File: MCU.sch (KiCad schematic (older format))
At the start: 18 parts, among them U4 STM32F303RETx

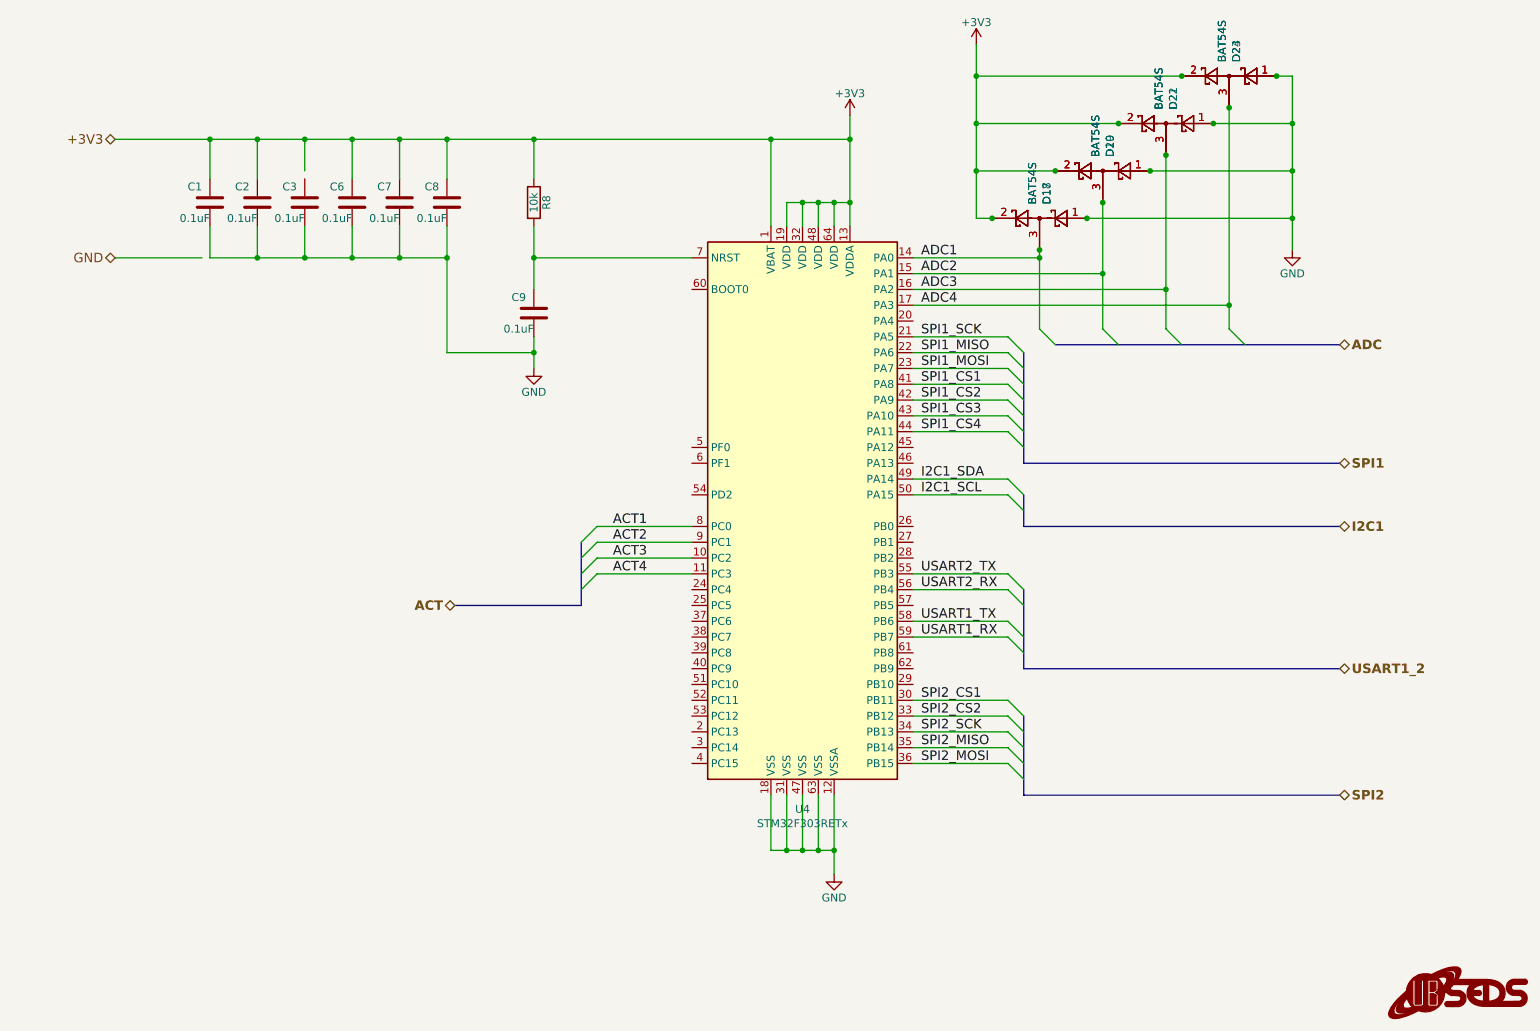
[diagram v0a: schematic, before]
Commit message: Updated pinmap
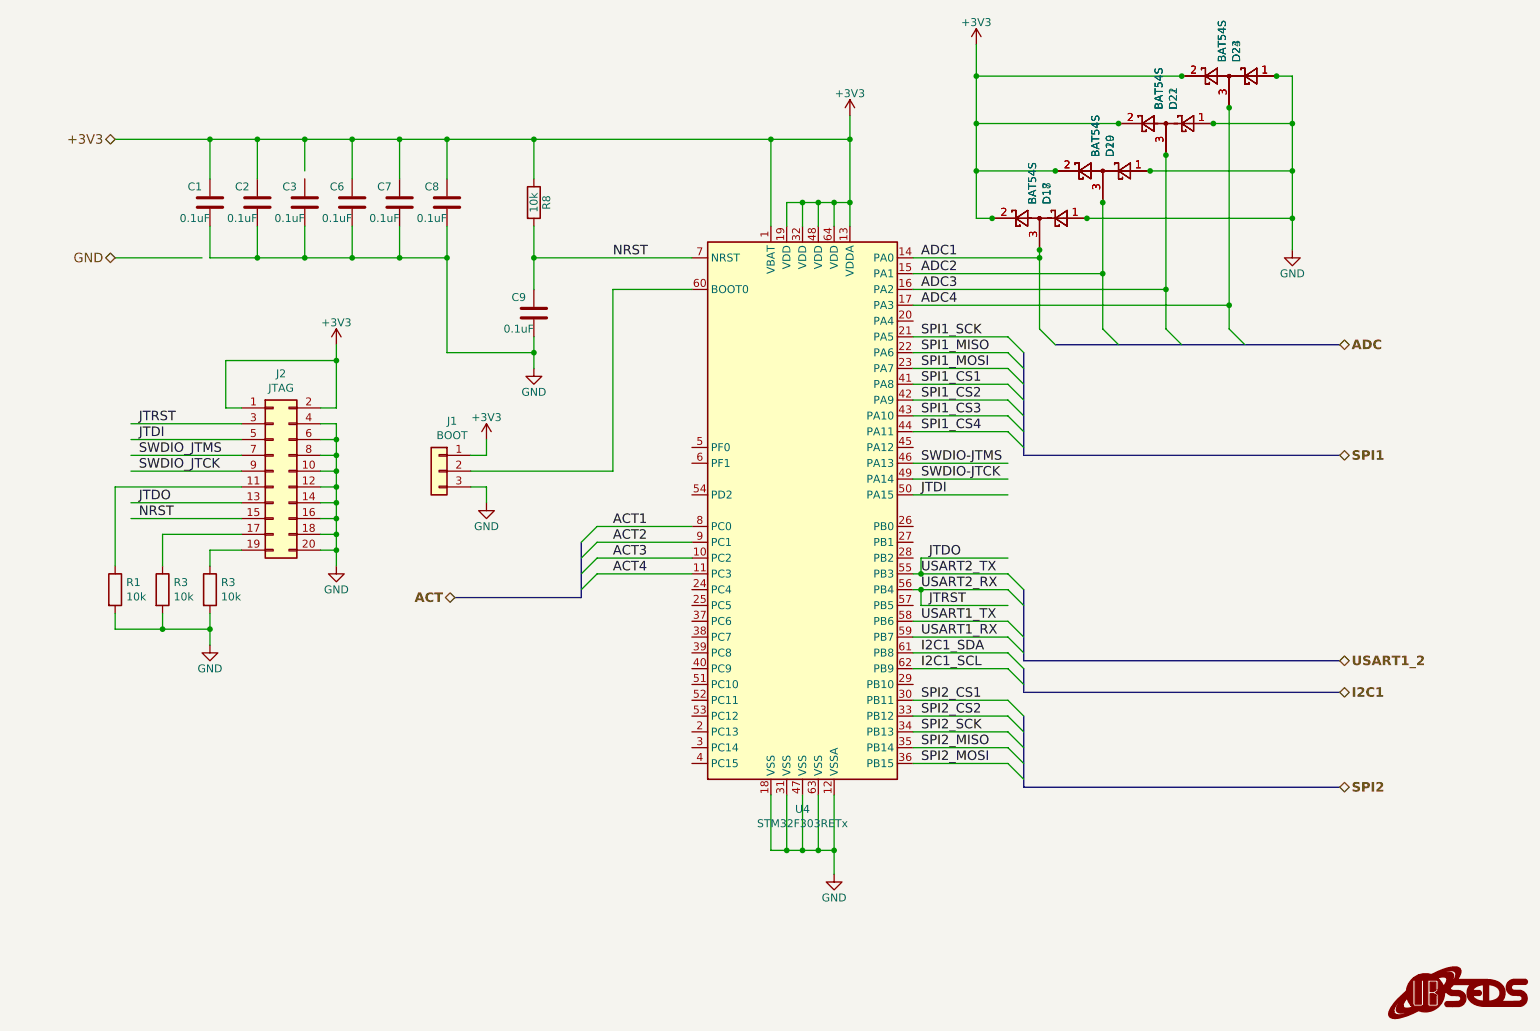
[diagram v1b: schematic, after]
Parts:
- added J1: BOOT, symbol Connector_Generic:Conn_01x03
- added J2: JTAG, symbol Connector_Generic:Conn_02x10_Odd_Even
- added R1, R3 (x2): 10k, symbol Device:R
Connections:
- net labels added: JTDI, JTDO, JTRST, NRST, SWDIO-JTCK, SWDIO-JTMS, SWDIO_JTCK, SWDIO_JTMS
- wire segments 107 -> 165

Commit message: Starting to fix ERC errors
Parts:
- C3: renamed from C1; footprint (none) -> Capacitor_SMD:C_0603_1608Metric_Pad1.05x0.95mm_HandSolder
- C4: renamed from C2; footprint (none) -> Capacitor_SMD:C_0603_1608Metric_Pad1.05x0.95mm_HandSolder
- C5: renamed from C3; footprint (none) -> Capacitor_SMD:C_0603_1608Metric_Pad1.05x0.95mm_HandSolder
- C6, C7, C8, C9: footprint (none) -> Capacitor_SMD:C_0603_1608Metric_Pad1.05x0.95mm_HandSolder
- J2: footprint (none) -> Connector_PinHeader_2.54mm:PinHeader_2x10_P2.54mm_Vertical
- J3: renamed from J1; footprint (none) -> Connector_PinHeader_2.54mm:PinHeader_1x03_P2.54mm_Vertical
- R5: renamed from R1; footprint (none) -> Resistor_SMD:R_1206_3216Metric_Pad1.42x1.75mm_HandSolder
- R6, R7: renamed from R3; footprint (none) -> Resistor_SMD:R_1206_3216Metric_Pad1.42x1.75mm_HandSolder
- R8: footprint Resistor_THT:R_Axial_DIN0207_L6.3mm_D2.5mm_P10.16mm_Horizontal -> Resistor_SMD:R_1206_3216Metric_Pad1.42x1.75mm_HandSolder
- renumbered D17 to D1, D18 to D2, D19 to D3, D20 to D4, D21 to D5, D22 to D6, D23 to D7, D24 to D8, U4 to U6
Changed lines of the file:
@@
 $Descr USLetter 11000 8500
 encoding utf-8
-Sheet 3 3
+Sheet 2 3
 Title "Flight Computer"
 Date ""
@@
 $EndComp
 $Comp
-L MCU_ST_STM32F3:STM32F303RETx U4
+L MCU_ST_STM32F3:STM32F303RETx U6
 U 1 1 5DF0B287
 P 5700 4050
-F 0 "U4" H 5700 2161 50  0000 C CNN
+F 0 "U6" H 5700 2161 50  0000 C CNN
 F 1 "STM32F303RETx" H 5700 2070 50  0000 C CNN
 F 2 "Package_QFP:LQFP-64_10x10mm_P0.5mm" H 5100 2350 50  0001 R CNN
@@
 $EndComp
 $Comp
-L power:+3V3 #PWR0123
+L power:+3V3 #PWR030
 U 1 1 5DF125E2
 P 6000 1550
-F 0 "#PWR0123" H 6000 1400 50  0001 C CNN
+F 0 "#PWR030" H 6000 1400 50  0001 C CNN
 F 1 "+3V3" H 6000 1690 50  0000 C CNN
 F 2 "" H 6000 1550 50  0001 C CNN
@@
 $EndComp
 $Comp
-L power:GND #PWR0124
+L power:GND #PWR029
 U 1 1 5DF17C0F
 P 5900 6350
-F 0 "#PWR0124" H 5900 6100 50  0001 C CNN
+F 0 "#PWR029" H 5900 6100 50  0001 C CNN
 F 1 "GND" H 5900 6200 50  0000 C CNN
 F 2 "" H 5900 6350 50  0001 C CNN
@@
 	5500 1700 5500 2250
 $Comp
-L power:GND #PWR0125
+L power:GND #PWR028
 U 1 1 5DFA0210
 P 4000 3150
-F 0 "#PWR0125" H 4000 2900 50  0001 C CNN
+F 0 "#PWR028" H 4000 2900 50  0001 C CNN
 F 1 "GND" H 4000 3000 50  0000 C CNN
 F 2 "" H 4000 3150 50  0001 C CNN
@@
 	7000 3550 7100 3650
 $Comp
-L Diode:BAT54S D19
+L Diode:BAT54S D3
 U 1 1 5E142556
 P 7600 1900
-F 0 "D19" V 7554 1988 50  0000 L CNN
+F 0 "D3" V 7554 1988 50  0000 L CNN
 F 1 "BAT54S" V 7645 1988 50  0000 L CNN
 F 2 "Package_TO_SOT_SMD:SOT-23" H 7675 2025 50  0001 L CNN
@@
 $EndComp
 $Comp
-L Diode:BAT54S D20
+L Diode:BAT54S D4
 U 1 1 5E14255C
 P 7600 1900
-F 0 "D20" V 7554 1988 50  0000 L CNN
+F 0 "D4" V 7554 1988 50  0000 L CNN
 F 1 "BAT54S" V 7645 1988 50  0000 L CNN
 F 2 "Package_TO_SOT_SMD:SOT-23" H 7675 2025 50  0001 L CNN
@@
 $EndComp
 $Comp
-L Diode:BAT54S D21
+L Diode:BAT54S D5
 U 1 1 5E211E6E
 P 8000 1600
-F 0 "D21" V 7954 1688 50  0000 L CNN
+F 0 "D5" V 7954 1688 50  0000 L CNN
 F 1 "BAT54S" V 8045 1688 50  0000 L CNN
 F 2 "Package_TO_SOT_SMD:SOT-23" H 8075 1725 50  0001 L CNN
@@
 $EndComp
 $Comp
-L Diode:BAT54S D22
+L Diode:BAT54S D6
 U 1 1 5E211E6F
 P 8000 1600
-F 0 "D22" V 7954 1688 50  0000 L CNN
+F 0 "D6" V 7954 1688 50  0000 L CNN
 F 1 "BAT54S" V 8045 1688 50  0000 L CNN
 F 2 "Package_TO_SOT_SMD:SOT-23" H 8075 1725 50  0001 L CNN
@@
 $EndComp
 $Comp
-L power:+3V3 #PWR0126
+L power:+3V3 #PWR031
 U 1 1 5E211E72
 P 6800 1100
-F 0 "#PWR0126" H 6800 950 50  0001 C CNN
+F 0 "#PWR031" H 6800 950 50  0001 C CNN
 F 1 "+3V3" H 6800 1240 50  0000 C CNN
 F 2 "" H 6800 1100 50  0001 C CNN
@@
 $EndComp
 $Comp
-L power:GND #PWR0127
+L power:GND #PWR032
 U 1 1 5E211E73
 P 8800 2400
-F 0 "#PWR0127" H 8800 2150 50  0001 C CNN
+F 0 "#PWR032" H 8800 2150 50  0001 C CNN
 F 1 "GND" H 8800 2250 50  0000 C CNN
 F 2 "" H 8800 2400 50  0001 C CNN
@@
 $EndComp
 $Comp
-L Diode:BAT54S D18
+L Diode:BAT54S D2
 U 1 1 5E211E6B
 P 7200 2200
-F 0 "D18" V 7154 2288 50  0000 L CNN
+F 0 "D2" V 7154 2288 50  0000 L CNN
 F 1 "BAT54S" V 7245 2288 50  0000 L CNN
 F 2 "Package_TO_SOT_SMD:SOT-23" H 7275 2325 50  0001 L CNN
@@
 $EndComp
 $Comp
-L Diode:BAT54S D17
+L Diode:BAT54S D1
 U 1 1 5E211E6A
 P 7200 2200
-F 0 "D17" V 7154 2288 50  0000 L CNN
+F 0 "D1" V 7154 2288 50  0000 L CNN
 F 1 "BAT54S" V 7245 2288 50  0000 L CNN
 F 2 "Package_TO_SOT_SMD:SOT-23" H 7275 2325 50  0001 L CNN
@@
 $EndComp
 $Comp
-L Diode:BAT54S D23
+L Diode:BAT54S D7
 U 1 1 5E211E70
 P 8400 1300
-F 0 "D23" V 8354 1388 50  0000 L CNN
+F 0 "D7" V 8354 1388 50  0000 L CNN
 F 1 "BAT54S" V 8445 1388 50  0000 L CNN
 F 2 "Package_TO_SOT_SMD:SOT-23" H 8475 1425 50  0001 L CNN
@@
 $EndComp
 $Comp
-L Diode:BAT54S D24
+L Diode:BAT54S D8
 U 1 1 5E211E71
 P 8400 1300
-F 0 "D24" V 8354 1388 50  0000 L CNN
+F 0 "D8" V 8354 1388 50  0000 L CNN
 F 1 "BAT54S" V 8445 1388 50  0000 L CNN
 F 2 "Package_TO_SOT_SMD:SOT-23" H 8475 1425 50  0001 L CNN
@@
 F 0 "C9" H 4050 2700 50  0000 L CNN
 F 1 "0.1uF" H 4000 2900 50  0000 L CNN
-F 2 "" H 4038 2650 50  0001 C CNN
+F 2 "Capacitor_SMD:C_0603_1608Metric_Pad1.05x0.95mm_HandSolder" H 4038 2650 50  0001 C CNN
 F 3 "" H 4000 2800 50  0001 C CNN
 	1    4000 2800
@@
 F 0 "C8" H 3500 2000 50  0000 L CNN
 F 1 "0.1uF" H 3450 2200 50  0000 L CNN
-F 2 "" H 3488 1950 50  0001 C CNN
+F 2 "Capacitor_SMD:C_0603_1608Metric_Pad1.05x0.95mm_HandSolder" H 3488 1950 50  0001 C CNN
 F 3 "" H 3450 2100 50  0001 C CNN
 	1    3450 2100
@@
 F 0 "R8" V 4080 2100 50  0000 C CNN
 F 1 "10k" V 4000 2100 50  0000 C CNN
-F 2 "Resistor_THT:R_Axial_DIN0207_L6.3mm_D2.5mm_P10.16mm_Horizontal" V 3930 2100 50  0001 C CNN
+F 2 "Resistor_SMD:R_1206_3216Metric_Pad1.42x1.75mm_HandSolder" V 3930 2100 50  0001 C CNN
 F 3 "" H 4000 2100 50  0001 C CNN
 	1    4000 2100
@@
 F 0 "C7" H 3200 2000 50  0000 L CNN
 F 1 "0.1uF" H 3150 2200 50  0000 L CNN
-F 2 "" H 3188 1950 50  0001 C CNN
+F 2 "Capacitor_SMD:C_0603_1608Metric_Pad1.05x0.95mm_HandSolder" H 3188 1950 50  0001 C CNN
 F 3 "" H 3150 2100 50  0001 C CNN
 	1    3150 2100
@@
 F 0 "C6" H 2900 2000 50  0000 L CNN
 F 1 "0.1uF" H 2850 2200 50  0000 L CNN
-F 2 "" H 2888 1950 50  0001 C CNN
+F 2 "Capacitor_SMD:C_0603_1608Metric_Pad1.05x0.95mm_HandSolder" H 2888 1950 50  0001 C CNN
 F 3 "" H 2850 2100 50  0001 C CNN
 	1    2850 2100
@@
 $EndComp
 $Comp
-L Device:C C3
+L Device:C C5
 U 1 1 5E27DD3C
 P 2550 2100
-F 0 "C3" H 2600 2000 50  0000 L CNN
+F 0 "C5" H 2600 2000 50  0000 L CNN
 F 1 "0.1uF" H 2550 2200 50  0000 L CNN
-F 2 "" H 2588 1950 50  0001 C CNN
+F 2 "Capacitor_SMD:C_0603_1608Metric_Pad1.05x0.95mm_HandSolder" H 2588 1950 50  0001 C CNN
 F 3 "" H 2550 2100 50  0001 C CNN
 	1    2550 2100
@@
 $EndComp
 $Comp
-L Device:C C2
+L Device:C C4
 U 1 1 5E2843FA
 P 2250 2100
-F 0 "C2" H 2300 2000 50  0000 L CNN
+F 0 "C4" H 2300 2000 50  0000 L CNN
 F 1 "0.1uF" H 2250 2200 50  0000 L CNN
-F 2 "" H 2288 1950 50  0001 C CNN
+F 2 "Capacitor_SMD:C_0603_1608Metric_Pad1.05x0.95mm_HandSolder" H 2288 1950 50  0001 C CNN
 F 3 "" H 2250 2100 50  0001 C CNN
 	1    2250 2100
@@
 $EndComp
 $Comp
-L Device:C C1
+L Device:C C3
 U 1 1 5E284400
 P 1950 2100
-F 0 "C1" H 2000 2000 50  0000 L CNN
+F 0 "C3" H 2000 2000 50  0000 L CNN
 F 1 "0.1uF" H 1950 2200 50  0000 L CNN
-F 2 "" H 1988 1950 50  0001 C CNN
+F 2 "Capacitor_SMD:C_0603_1608Metric_Pad1.05x0.95mm_HandSolder" H 1988 1950 50  0001 C CNN
 F 3 "" H 1950 2100 50  0001 C CNN
 	1    1950 2100
@@
 	2850 1700 3150 1700
 Connection ~ 3150 1700
-Wire Wire Line
-	2550 1900 2550 1700
 Wire Wire Line
 	2550 1700 2850 1700
@@
 	1950 1700 1350 1700
 Connection ~ 1950 1700
-Wire Wire Line
-	1900 2450 1350 2450
 Text HLabel 1350 1700 0    60   BiDi ~ 0
 +3V3
@@
 	7100 5800 9100 5800
 $Comp
-L Connector_Generic:Conn_01x03 J1
+L Connector_Generic:Conn_01x03 J3
 U 1 1 5E38538A
 P 3400 3800
-F 0 "J1" H 3318 4117 50  0000 C CNN
+F 0 "J3" H 3318 4117 50  0000 C CNN
 F 1 "BOOT" H 3318 4026 50  0000 C CNN
-F 2 "" H 3400 3800 50  0001 C CNN
+F 2 "Connector_PinHeader_2.54mm:PinHeader_1x03_P2.54mm_Vertical" H 3400 3800 50  0001 C CNN
 F 3 "~" H 3400 3800 50  0001 C CNN
 	1    3400 3800
@@
 	3700 3900 3700 4000
 $Comp
-L power:GND #PWR?
+L power:GND #PWR027
 U 1 1 5E39962F
 P 3700 4000
-F 0 "#PWR?" H 3700 3750 50  0001 C CNN
+F 0 "#PWR027" H 3700 3750 50  0001 C CNN
 F 1 "GND" H 3700 3850 50  0000 C CNN
 F 2 "" H 3700 4000 50  0001 C CNN
@@
 $EndComp
 $Comp
-L power:+3V3 #PWR?
+L power:+3V3 #PWR026
 U 1 1 5E3A0F34
 P 3700 3600
-F 0 "#PWR?" H 3700 3450 50  0001 C CNN
+F 0 "#PWR026" H 3700 3450 50  0001 C CNN
 F 1 "+3V3" H 3700 3740 50  0000 C CNN
 F 2 "" H 3700 3600 50  0001 C CNN
@@
 F 0 "J2" H 2400 4417 50  0000 C CNN
 F 1 "JTAG" H 2400 4326 50  0000 C CNN
-F 2 "" H 2350 3800 50  0001 C CNN
+F 2 "Connector_PinHeader_2.54mm:PinHeader_2x10_P2.54mm_Vertical" H 2350 3800 50  0001 C CNN
 F 3 "~" H 2350 3800 50  0001 C CNN
 	1    2350 3800
@@
 $EndComp
 $Comp
-L power:GND #PWR?
+L power:GND #PWR025
 U 1 1 5E3B7BFA
 P 2750 4400
-F 0 "#PWR?" H 2750 4150 50  0001 C CNN
+F 0 "#PWR025" H 2750 4150 50  0001 C CNN
 F 1 "GND" H 2750 4250 50  0000 C CNN
 F 2 "" H 2750 4400 50  0001 C CNN
@@
 $EndComp
 $Comp
-L power:+3V3 #PWR?
+L power:+3V3 #PWR024
 U 1 1 5E3BE166
 P 2750 3000
-F 0 "#PWR?" H 2750 2850 50  0001 C CNN
+F 0 "#PWR024" H 2750 2850 50  0001 C CNN
 F 1 "+3V3" H 2750 3140 50  0000 C CNN
 F 2 "" H 2750 3000 50  0001 C CNN
@@
 	2750 3600 2750 3700
 $Comp
-L Device:R R3
+L Device:R R7
 U 1 1 5E40139B
 P 1950 4550
-F 0 "R3" H 2020 4596 50  0000 L CNN
+F 0 "R7" H 2020 4596 50  0000 L CNN
 F 1 "10k" H 2020 4505 50  0000 L CNN
-F 2 "" V 1880 4550 50  0001 C CNN
+F 2 "Resistor_SMD:R_1206_3216Metric_Pad1.42x1.75mm_HandSolder" V 1880 4550 50  0001 C CNN
 F 3 "~" H 1950 4550 50  0001 C CNN
 	1    1950 4550
@@
 $EndComp
 $Comp
-L Device:R R3
+L Device:R R6
 U 1 1 5E40263A
 P 1650 4550
-F 0 "R3" H 1720 4596 50  0000 L CNN
+F 0 "R6" H 1720 4596 50  0000 L CNN
 F 1 "10k" H 1720 4505 50  0000 L CNN
-F 2 "" V 1580 4550 50  0001 C CNN
+F 2 "Resistor_SMD:R_1206_3216Metric_Pad1.42x1.75mm_HandSolder" V 1580 4550 50  0001 C CNN
 F 3 "~" H 1650 4550 50  0001 C CNN
 	1    1650 4550
@@
 $EndComp
 $Comp
-L Device:R R1
+L Device:R R5
 U 1 1 5E4081A2
 P 1350 4550
-F 0 "R1" H 1420 4596 50  0000 L CNN
+F 0 "R5" H 1420 4596 50  0000 L CNN
 F 1 "10k" H 1420 4505 50  0000 L CNN
-F 2 "" V 1280 4550 50  0001 C CNN
+F 2 "Resistor_SMD:R_1206_3216Metric_Pad1.42x1.75mm_HandSolder" V 1280 4550 50  0001 C CNN
 F 3 "~" H 1350 4550 50  0001 C CNN
 	1    1350 4550
@@
 $EndComp
 $Comp
-L power:GND #PWR?
+L power:GND #PWR023
 U 1 1 5E40ED05
 P 1950 4900
-F 0 "#PWR?" H 1950 4650 50  0001 C CNN
+F 0 "#PWR023" H 1950 4650 50  0001 C CNN
 F 1 "GND" H 1950 4750 50  0000 C CNN
 F 2 "" H 1950 4900 50  0001 C CNN
@@
 Text Label 1500 4100 0    60   ~ 0
 NRST
+Wire Wire Line
+	1350 2450 1950 2450
+Connection ~ 1950 2450
+Wire Wire Line
+	2550 1700 2550 1950
 Wire Bus Line
 	7100 5050 7100 5200
